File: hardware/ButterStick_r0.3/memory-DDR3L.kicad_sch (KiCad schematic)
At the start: 0 parts

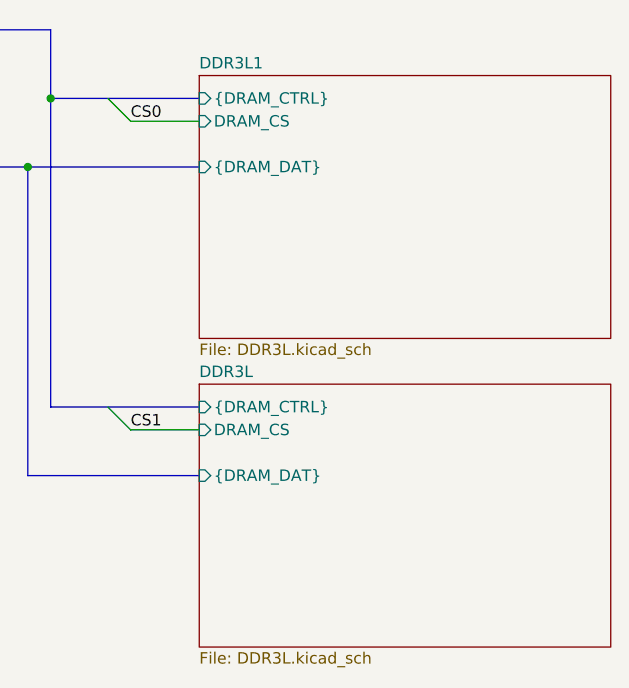
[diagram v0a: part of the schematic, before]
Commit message: hw.r0_3: routing improvements
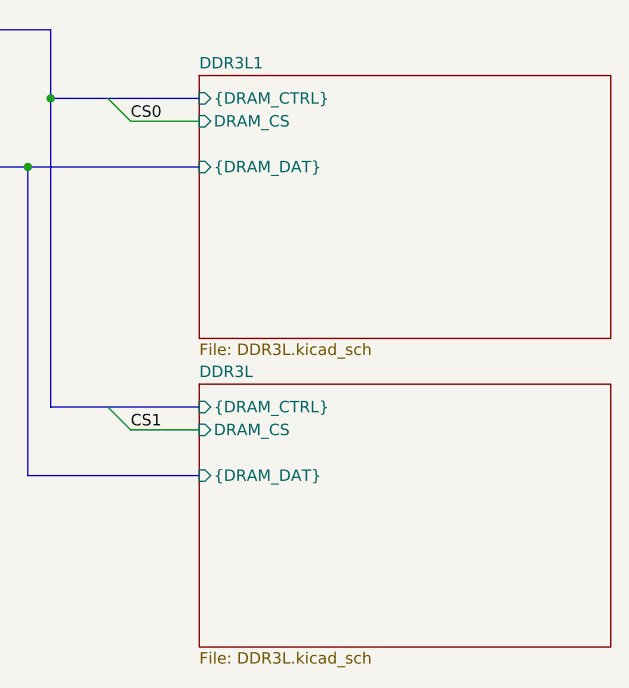
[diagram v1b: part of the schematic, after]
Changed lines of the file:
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@@
 (kicad_sch (version 20200512) (host eeschema "5.99.0-unknown-c8476d6~101~ubuntu18.04.1")
-  (page 13 20)
+  (page 1 20)
   (paper "A4")
   (title_block
@@
   )
   (sheet (at 87.63 115.57) (size 45.72 29.21)
+    (stroke (width 0.1524) (color 132 0 132 1))
+    (fill (color 255 255 255 1.0000))
     (property "Sheet name" "DDR3L" (id 0) (at 87.63 114.9345 0)
       (effects (font (size 1.27 1.27)) (justify left bottom))
@@
   )
   (sheet (at 87.63 81.28) (size 45.72 29.21)
+    (stroke (width 0.1524) (color 132 0 132 1))
+    (fill (color 255 255 255 1.0000))
     (property "Sheet name" "DDR3L1" (id 0) (at 87.63 80.6445 0)
       (effects (font (size 1.27 1.27)) (justify left bottom))

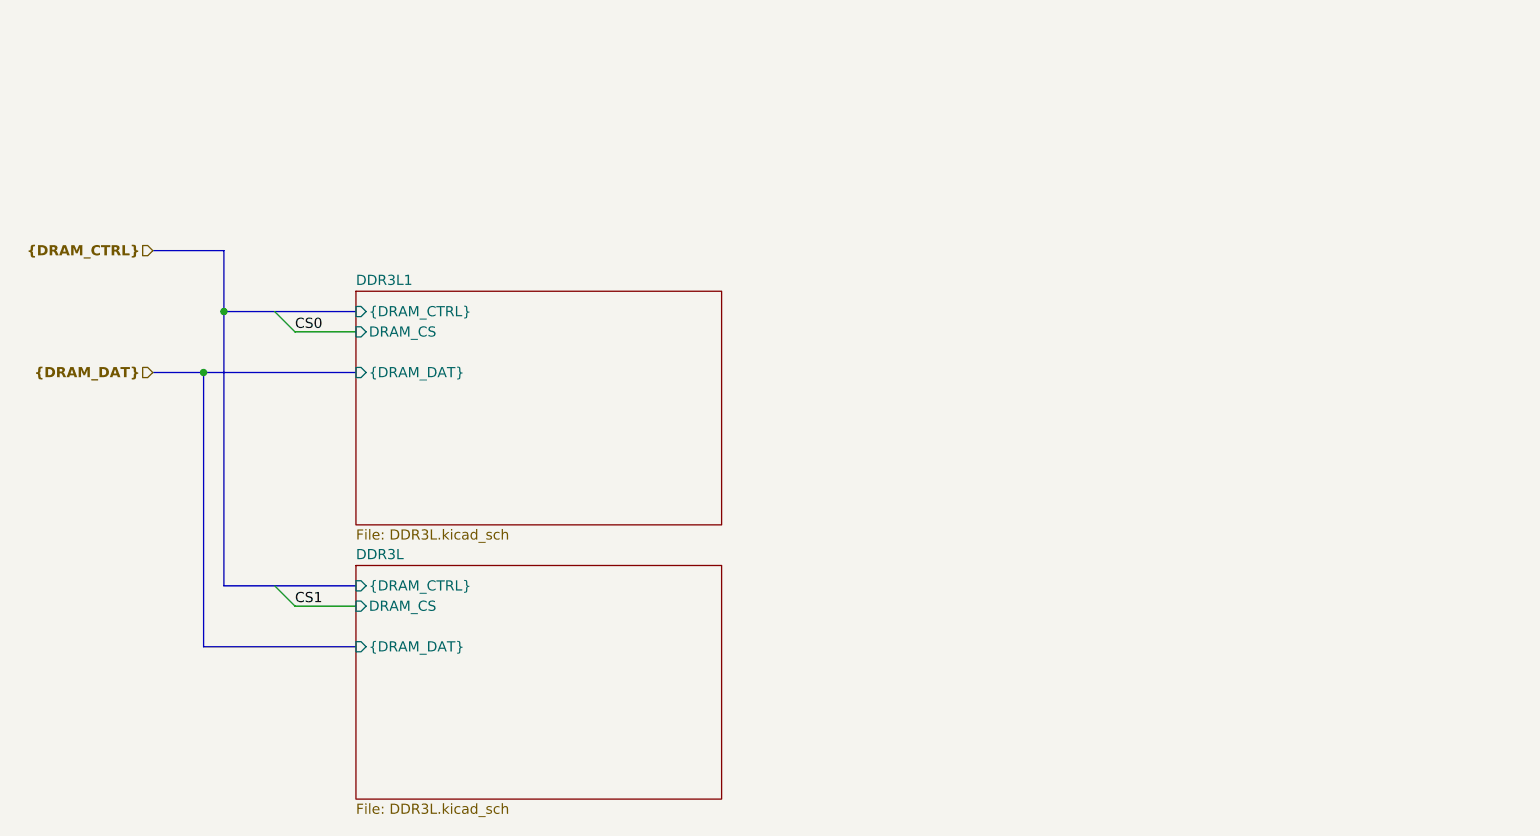
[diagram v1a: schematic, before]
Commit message: hw.r0_3: Start routing DDR3 interface
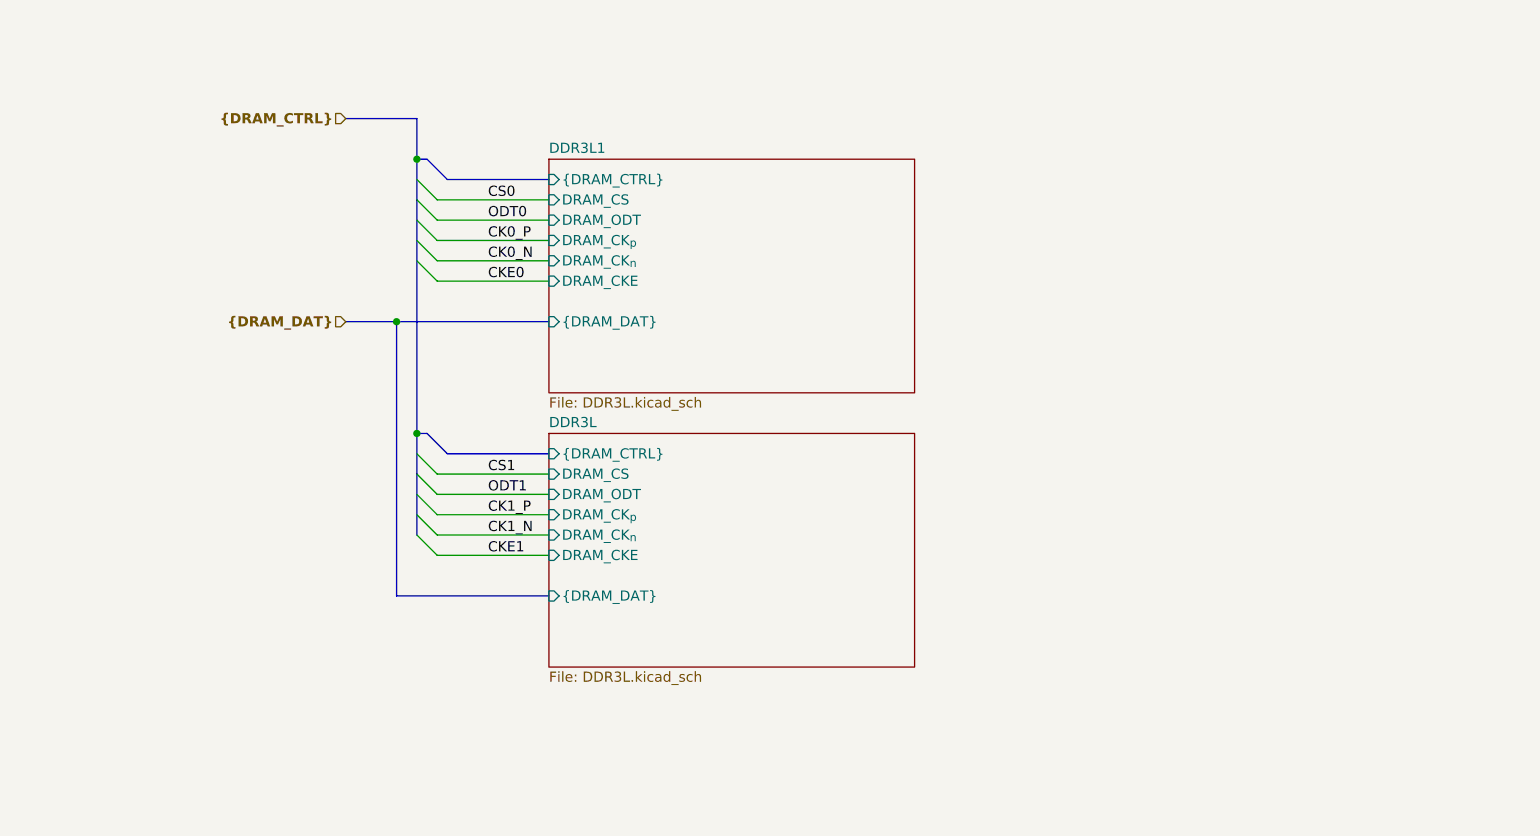
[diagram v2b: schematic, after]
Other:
- sheet DDR3L ports: added DRAM_CKE, DRAM_CK_{n}, DRAM_CK_{p}, DRAM_ODT; removed none
- sheet DDR3L1 ports: added DRAM_CKE, DRAM_CK_{n}, DRAM_CK_{p}, DRAM_ODT; removed none
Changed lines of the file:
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@@
-(kicad_sch (version 20200512) (host eeschema "5.99.0-unknown-c8476d6~101~ubuntu18.04.1")
+(kicad_sch (version 20200512) (host eeschema "5.99.0-unknown-711fc99~101~ubuntu18.04.1")
   (page 1 20)
   (paper "A4")
@@
     (company "GsD")
   )
-  (junction (at 68.58 91.44))
-  (junction (at 71.12 83.82))
-  (bus_entry (at 77.47 83.82) (size 2.54 2.54))
-  (bus_entry (at 77.47 118.11) (size 2.54 2.54))
-  (wire (pts (xy 80.01 86.36) (xy 87.63 86.36)))
-  (wire (pts (xy 80.01 120.65) (xy 87.63 120.65)))
-  (bus (pts (xy 62.23 76.2) (xy 71.12 76.2)))
-  (bus (pts (xy 62.23 91.44) (xy 68.58 91.44)))
-  (bus (pts (xy 68.58 91.44) (xy 68.58 125.73)))
-  (bus (pts (xy 68.58 91.44) (xy 87.63 91.44)))
-  (bus (pts (xy 68.58 125.73) (xy 87.63 125.73)))
-  (bus (pts (xy 71.12 83.82) (xy 71.12 76.2)))
-  (bus (pts (xy 71.12 83.82) (xy 71.12 118.11)))
-  (bus (pts (xy 71.12 83.82) (xy 87.63 83.82)))
-  (bus (pts (xy 71.12 118.11) (xy 87.63 118.11)))
-  (label "CS0" (at 80.01 86.36 0)
+  (junction (at 92.71 85.09))
+  (junction (at 95.25 64.77))
+  (junction (at 95.25 99.06))
+  (bus_entry (at 95.25 67.31) (size 2.54 2.54))
+  (bus_entry (at 95.25 69.85) (size 2.54 2.54))
+  (bus_entry (at 95.25 72.39) (size 2.54 2.54))
+  (bus_entry (at 95.25 74.93) (size 2.54 2.54))
+  (bus_entry (at 95.25 77.47) (size 2.54 2.54))
+  (bus_entry (at 95.25 101.6) (size 2.54 2.54))
+  (bus_entry (at 95.25 104.14) (size 2.54 2.54))
+  (bus_entry (at 95.25 106.68) (size 2.54 2.54))
+  (bus_entry (at 95.25 109.22) (size 2.54 2.54))
+  (bus_entry (at 95.25 111.76) (size 2.54 2.54))
+  (wire (pts (xy 97.79 69.85) (xy 111.76 69.85)))
+  (wire (pts (xy 97.79 72.39) (xy 111.76 72.39)))
+  (wire (pts (xy 97.79 74.93) (xy 111.76 74.93)))
+  (wire (pts (xy 97.79 77.47) (xy 111.76 77.47)))
+  (wire (pts (xy 97.79 80.01) (xy 111.76 80.01)))
+  (wire (pts (xy 97.79 104.14) (xy 111.76 104.14)))
+  (wire (pts (xy 97.79 106.68) (xy 111.76 106.68)))
+  (wire (pts (xy 97.79 109.22) (xy 111.76 109.22)))
+  (wire (pts (xy 97.79 111.76) (xy 111.76 111.76)))
+  (wire (pts (xy 97.79 114.3) (xy 111.76 114.3)))
+  (bus (pts (xy 86.36 59.69) (xy 95.25 59.69)))
+  (bus (pts (xy 86.36 85.09) (xy 92.71 85.09)))
+  (bus (pts (xy 92.71 85.09) (xy 92.71 119.38)))
+  (bus (pts (xy 92.71 85.09) (xy 111.76 85.09)))
+  (bus (pts (xy 92.71 119.38) (xy 111.76 119.38)))
+  (bus (pts (xy 95.25 59.69) (xy 95.25 64.77)))
+  (bus (pts (xy 95.25 64.77) (xy 95.25 69.85)))
+  (bus (pts (xy 95.25 64.77) (xy 96.52 64.77)))
+  (bus (pts (xy 95.25 69.85) (xy 95.25 74.93)))
+  (bus (pts (xy 95.25 74.93) (xy 95.25 99.06)))
+  (bus (pts (xy 95.25 99.06) (xy 95.25 104.14)))
+  (bus (pts (xy 95.25 99.06) (xy 96.52 99.06)))
+  (bus (pts (xy 95.25 104.14) (xy 95.25 106.68)))
+  (bus (pts (xy 95.25 106.68) (xy 95.25 111.76)))
+  (bus (pts (xy 96.52 64.77) (xy 99.06 67.31)))
+  (bus (pts (xy 99.06 67.31) (xy 111.76 67.31)))
+  (bus (pts (xy 99.06 101.6) (xy 96.52 99.06)))
+  (bus (pts (xy 111.76 101.6) (xy 99.06 101.6)))
+  (label "CS0" (at 104.14 69.85 0)
     (effects (font (size 1.27 1.27)) (justify left bottom))
   )
-  (label "CS1" (at 80.01 120.65 0)
+  (label "ODT0" (at 104.14 72.39 0)
     (effects (font (size 1.27 1.27)) (justify left bottom))
   )
-  (hierarchical_label "{DRAM_CTRL}" (shape input) (at 62.23 76.2 180)
+  (label "CK0_P" (at 104.14 74.93 0)
+    (effects (font (size 1.27 1.27)) (justify left bottom))
+  )
+  (label "CK0_N" (at 104.14 77.47 0)
+    (effects (font (size 1.27 1.27)) (justify left bottom))
+  )
+  (label "CKE0" (at 104.14 80.01 0)
+    (effects (font (size 1.27 1.27)) (justify left bottom))
+  )
+  (label "CS1" (at 104.14 104.14 0)
+    (effects (font (size 1.27 1.27)) (justify left bottom))
+  )
+  (label "ODT1" (at 104.14 106.68 0)
+    (effects (font (size 1.27 1.27)) (justify left bottom))
+  )
+  (label "CK1_P" (at 104.14 109.22 0)
+    (effects (font (size 1.27 1.27)) (justify left bottom))
+  )
+  (label "CK1_N" (at 104.14 111.76 0)
+    (effects (font (size 1.27 1.27)) (justify left bottom))
+  )
+  (label "CKE1" (at 104.14 114.3 0)
+    (effects (font (size 1.27 1.27)) (justify left bottom))
+  )
+  (hierarchical_label "{DRAM_CTRL}" (shape input) (at 86.36 59.69 180)
     (effects (font (size 1.27 1.27) (thickness 0.254) bold) (justify right))
   )
-  (hierarchical_label "{DRAM_DAT}" (shape input) (at 62.23 91.44 180)
+  (hierarchical_label "{DRAM_DAT}" (shape input) (at 86.36 85.09 180)
     (effects (font (size 1.27 1.27) (thickness 0.254) bold) (justify right))
   )
-  (sheet (at 87.63 115.57) (size 45.72 29.21)
+  (sheet (at 111.76 99.06) (size 45.72 29.21)
     (stroke (width 0.1524) (color 132 0 132 1))
     (fill (color 255 255 255 1.0000))
-    (property "Sheet name" "DDR3L" (id 0) (at 87.63 114.9345 0)
+    (property "Sheet name" "DDR3L" (id 0) (at 111.76 98.4245 0)
       (effects (font (size 1.27 1.27)) (justify left bottom))
     )
-    (property "Sheet file" "DDR3L.kicad_sch" (id 1) (at 87.63 145.2885 0)
+    (property "Sheet file" "DDR3L.kicad_sch" (id 1) (at 111.76 128.7785 0)
       (effects (font (size 1.27 1.27)) (justify left top))
     )
-    (pin "{DRAM_DAT}" input (at 87.63 125.73 180)
+    (pin "{DRAM_DAT}" input (at 111.76 119.38 180)
       (effects (font (size 1.27 1.27)) (justify left))
     )
-    (pin "{DRAM_CTRL}" input (at 87.63 118.11 180)
+    (pin "{DRAM_CTRL}" input (at 111.76 101.6 180)
       (effects (font (size 1.27 1.27)) (justify left))
     )
-    (pin "DRAM_CS" input (at 87.63 120.65 180)
+    (pin "DRAM_CS" input (at 111.76 104.14 180)
+      (effects (font (size 1.27 1.27)) (justify left))
+    )
+    (pin "DRAM_ODT" input (at 111.76 106.68 180)
+      (effects (font (size 1.27 1.27)) (justify left))
+    )
+    (pin "DRAM_CK_{p}" input (at 111.76 109.22 180)
+      (effects (font (size 1.27 1.27)) (justify left))
+    )
+    (pin "DRAM_CK_{n}" input (at 111.76 111.76 180)
+      (effects (font (size 1.27 1.27)) (justify left))
+    )
+    (pin "DRAM_CKE" input (at 111.76 114.3 180)
       (effects (font (size 1.27 1.27)) (justify left))
     )
   )
-  (sheet (at 87.63 81.28) (size 45.72 29.21)
+  (sheet (at 111.76 64.77) (size 45.72 29.21)
     (stroke (width 0.1524) (color 132 0 132 1))
     (fill (color 255 255 255 1.0000))
-    (property "Sheet name" "DDR3L1" (id 0) (at 87.63 80.6445 0)
+    (property "Sheet name" "DDR3L1" (id 0) (at 111.76 64.1345 0)
       (effects (font (size 1.27 1.27)) (justify left bottom))
     )
-    (property "Sheet file" "DDR3L.kicad_sch" (id 1) (at 87.63 110.9985 0)
+    (property "Sheet file" "DDR3L.kicad_sch" (id 1) (at 111.76 94.4885 0)
       (effects (font (size 1.27 1.27)) (justify left top))
     )
-    (pin "{DRAM_DAT}" input (at 87.63 91.44 180)
+    (pin "{DRAM_DAT}" input (at 111.76 85.09 180)
       (effects (font (size 1.27 1.27)) (justify left))
     )
-    (pin "{DRAM_CTRL}" input (at 87.63 83.82 180)
+    (pin "{DRAM_CTRL}" input (at 111.76 67.31 180)
       (effects (font (size 1.27 1.27)) (justify left))
     )
-    (pin "DRAM_CS" input (at 87.63 86.36 180)
+    (pin "DRAM_CS" input (at 111.76 69.85 180)
       (effects (font (size 1.27 1.27)) (justify left))
     )
+    (pin "DRAM_ODT" input (at 111.76 72.39 180)
+      (effects (font (size 1.27 1.27)) (justify left))
+    )
+    (pin "DRAM_CK_{p}" input (at 111.76 74.93 180)
+      (effects (font (size 1.27 1.27)) (justify left))
+    )
+    (pin "DRAM_CK_{n}" input (at 111.76 77.47 180)
+      (effects (font (size 1.27 1.27)) (justify left))
+    )
+    (pin "DRAM_CKE" input (at 111.76 80.01 180)
+      (effects (font (size 1.27 1.27)) (justify left))
+    )

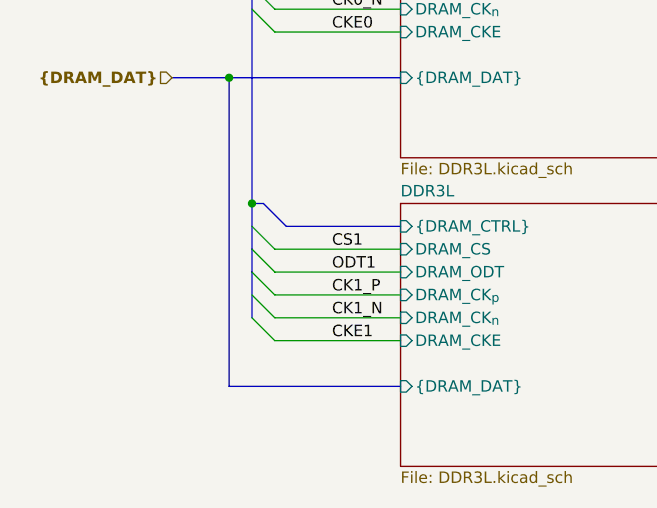
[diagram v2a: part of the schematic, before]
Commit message: hw.r0_3: Inital routing of DDR3 done
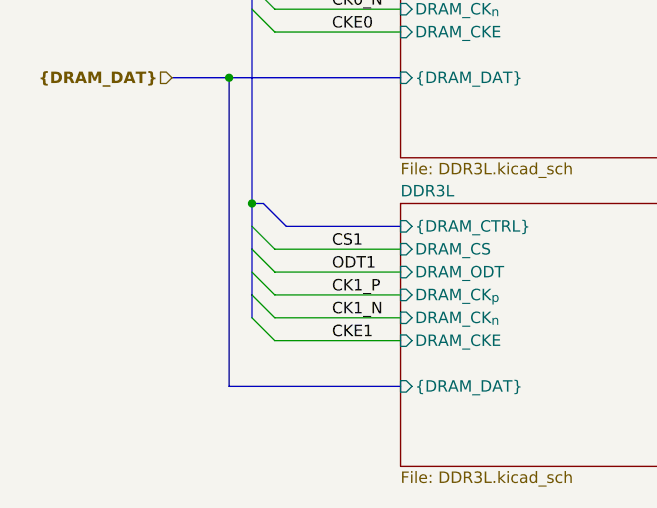
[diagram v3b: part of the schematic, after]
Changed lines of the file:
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@@
 (kicad_sch (version 20200512) (host eeschema "5.99.0-unknown-711fc99~101~ubuntu18.04.1")
-  (page 1 20)
+  (page 13 20)
   (paper "A4")
   (title_block
@@
   (bus (pts (xy 95.25 99.06) (xy 95.25 104.14)))
   (bus (pts (xy 95.25 99.06) (xy 96.52 99.06)))
-  (bus (pts (xy 95.25 104.14) (xy 95.25 106.68)))
-  (bus (pts (xy 95.25 106.68) (xy 95.25 111.76)))
+  (bus (pts (xy 95.25 104.14) (xy 95.25 109.22)))
+  (bus (pts (xy 95.25 109.22) (xy 95.25 111.76)))
   (bus (pts (xy 96.52 64.77) (xy 99.06 67.31)))
   (bus (pts (xy 99.06 67.31) (xy 111.76 67.31)))

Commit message: hw.r0_3: major blocks roughly routed
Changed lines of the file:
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@@
   (bus (pts (xy 95.25 99.06) (xy 95.25 104.14)))
   (bus (pts (xy 95.25 99.06) (xy 96.52 99.06)))
-  (bus (pts (xy 95.25 104.14) (xy 95.25 109.22)))
-  (bus (pts (xy 95.25 109.22) (xy 95.25 111.76)))
+  (bus (pts (xy 95.25 104.14) (xy 95.25 106.68)))
+  (bus (pts (xy 95.25 106.68) (xy 95.25 111.76)))
   (bus (pts (xy 96.52 64.77) (xy 99.06 67.31)))
   (bus (pts (xy 99.06 67.31) (xy 111.76 67.31)))
